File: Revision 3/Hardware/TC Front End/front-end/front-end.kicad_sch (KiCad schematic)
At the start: 0 parts

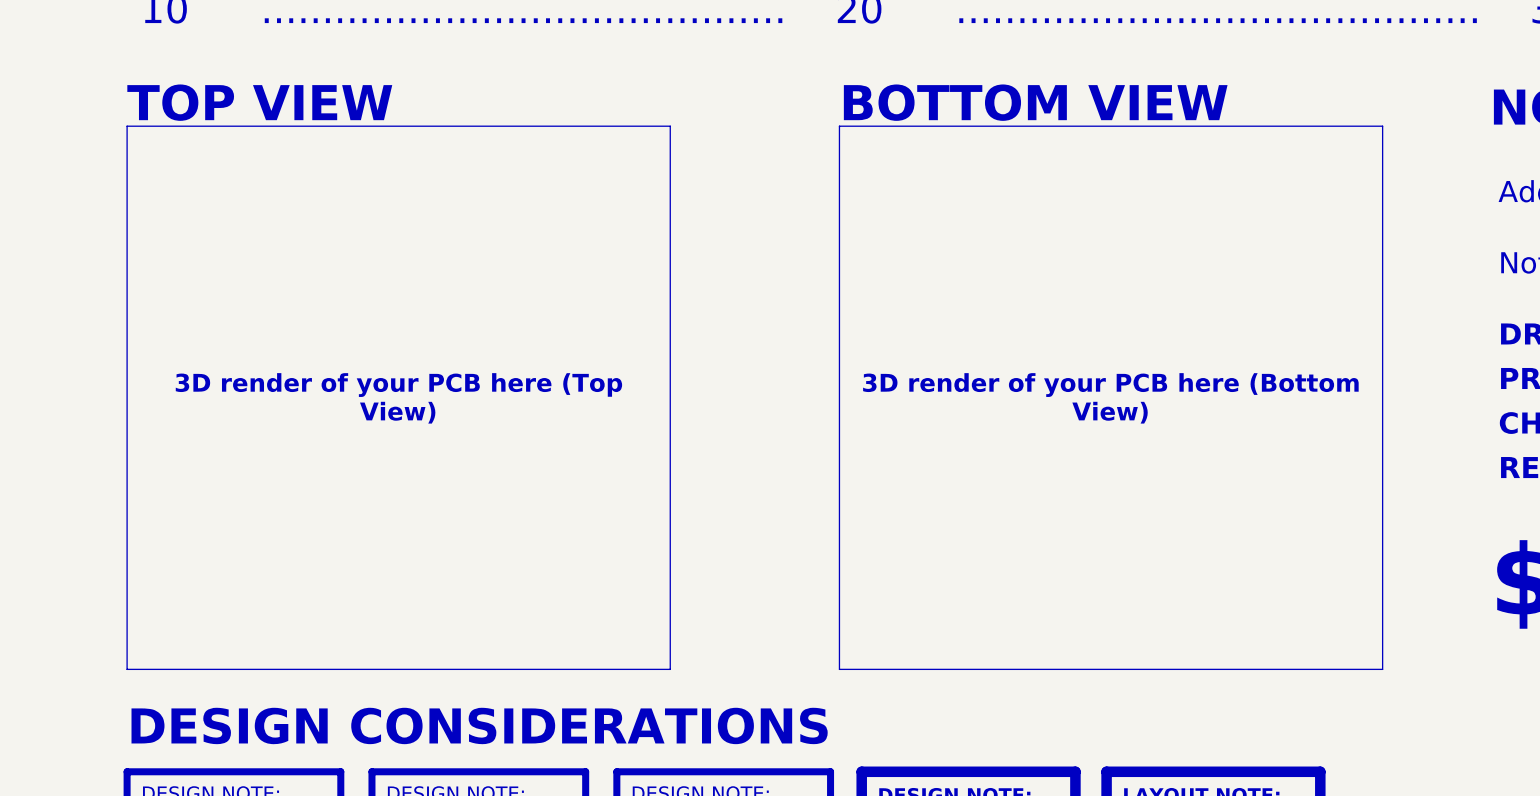
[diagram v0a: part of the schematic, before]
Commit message: Sent PCB to production, add images to schematic
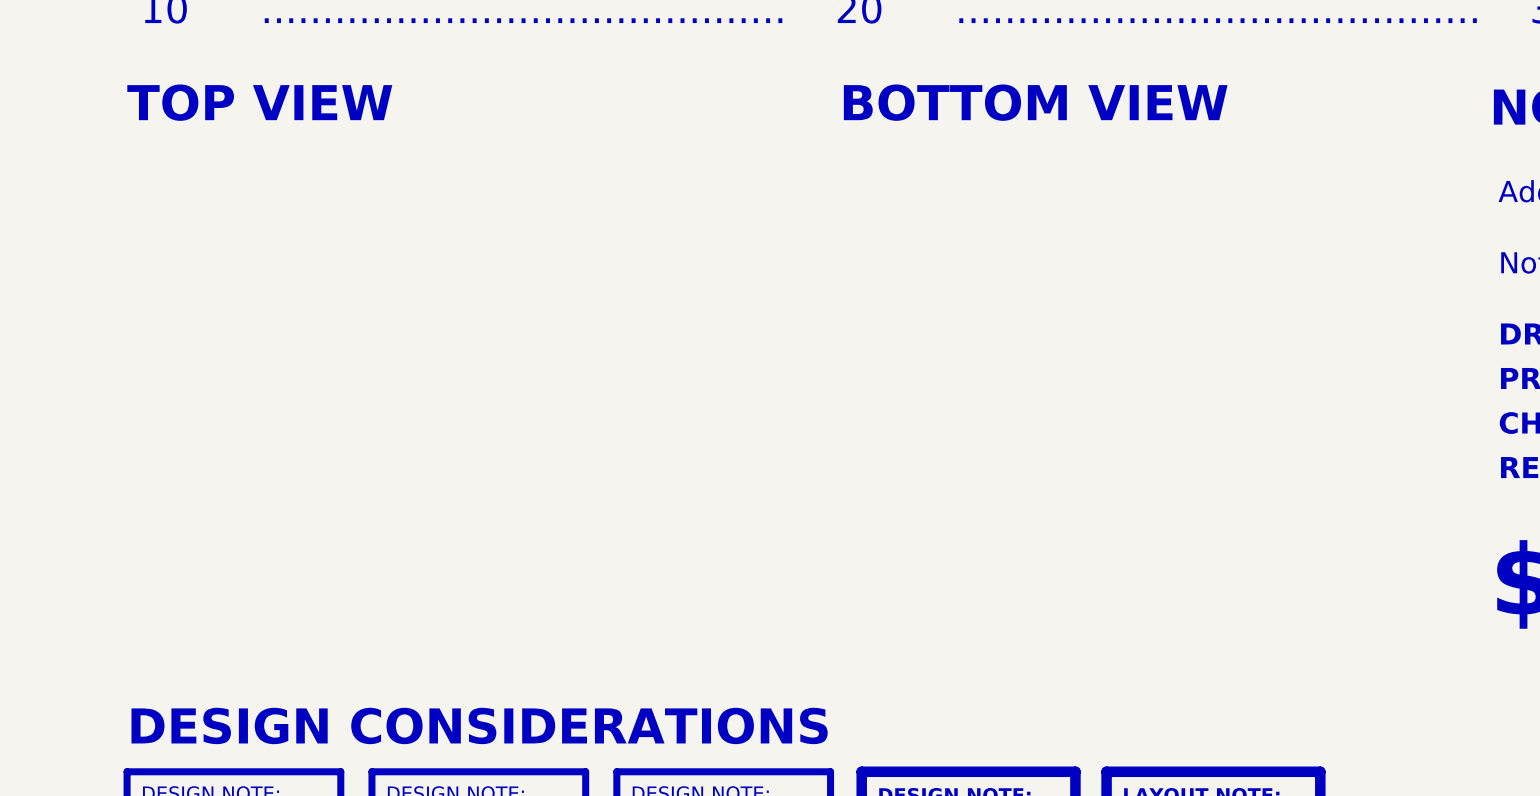
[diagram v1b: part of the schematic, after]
